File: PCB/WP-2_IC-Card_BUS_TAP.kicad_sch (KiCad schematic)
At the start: 4 parts, among them J1 SMS-138-01-G-S, J2 Conn_02x19_Odd_Even, J3 TMS-138-01

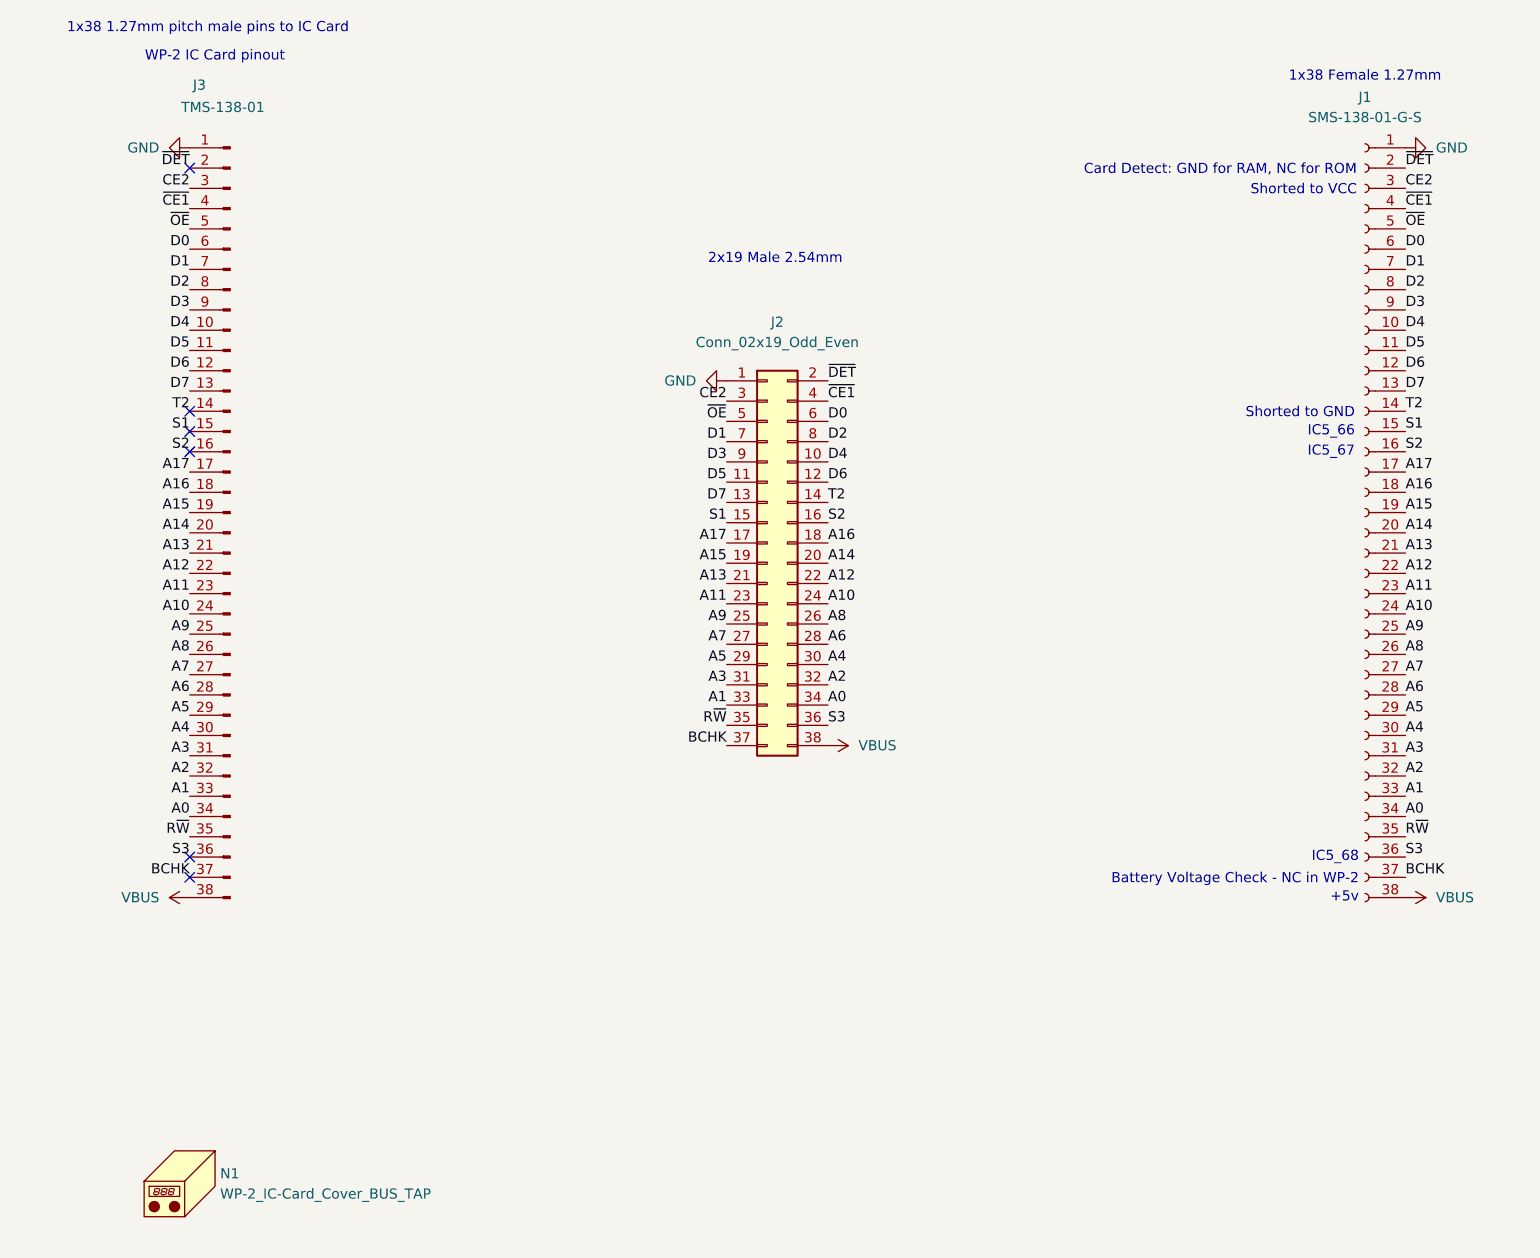
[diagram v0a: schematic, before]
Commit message: bus tap: 40p idc, extra gnd, breakout vcc to measure current
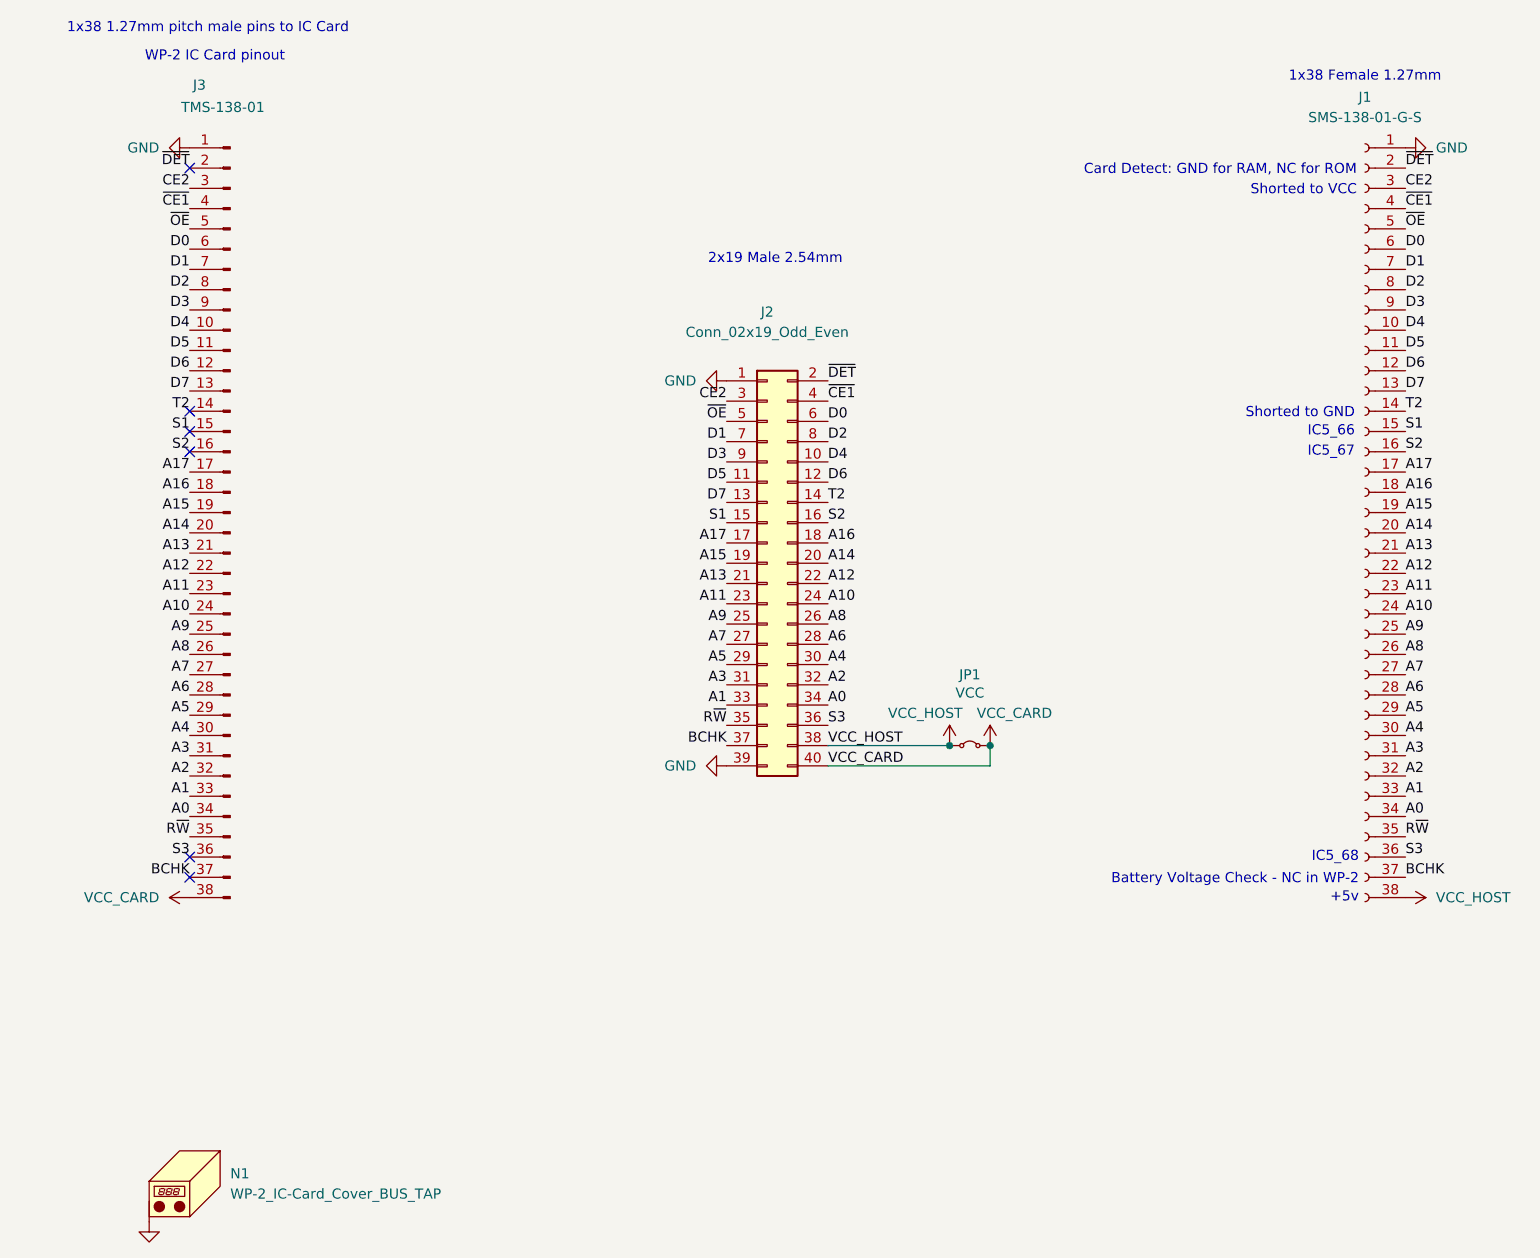
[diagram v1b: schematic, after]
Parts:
- added JP1: VCC, 000_LOCAL:PinHeader_1x02_P2.54mm_Vertical, symbol 000_LOCAL:Jumper_2_Small_Bridged
- J2: footprint 000_LOCAL:PinHeader_2x19_P2.54mm -> 000_LOCAL:PinHeader_2x20_P2.54mm; symbol 000_LOCAL:Conn_02x19_Odd_Even -> 000_LOCAL:Conn_02x20_Odd_Even
- N1: symbol 000_LOCAL:Housing -> 000_LOCAL:Housing_Pad; now in the parts list
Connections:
- net GND: now also J2.39 (Pin_39), N1.1 (PAD)
- net VBUS renamed VCC_HOST
- net VCC_HOST: now also JP1.1 (A); no longer J3.38 (Pin_38)
- new net VCC_CARD: J2.40 (Pin_40), J3.38 (Pin_38), JP1.2 (B)
